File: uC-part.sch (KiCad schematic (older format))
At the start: 21 parts, among them P1 swdio, Q1 Q_PNP_BCE, Q2 Q_PNP_BCE, U4 stm32f042k6tx

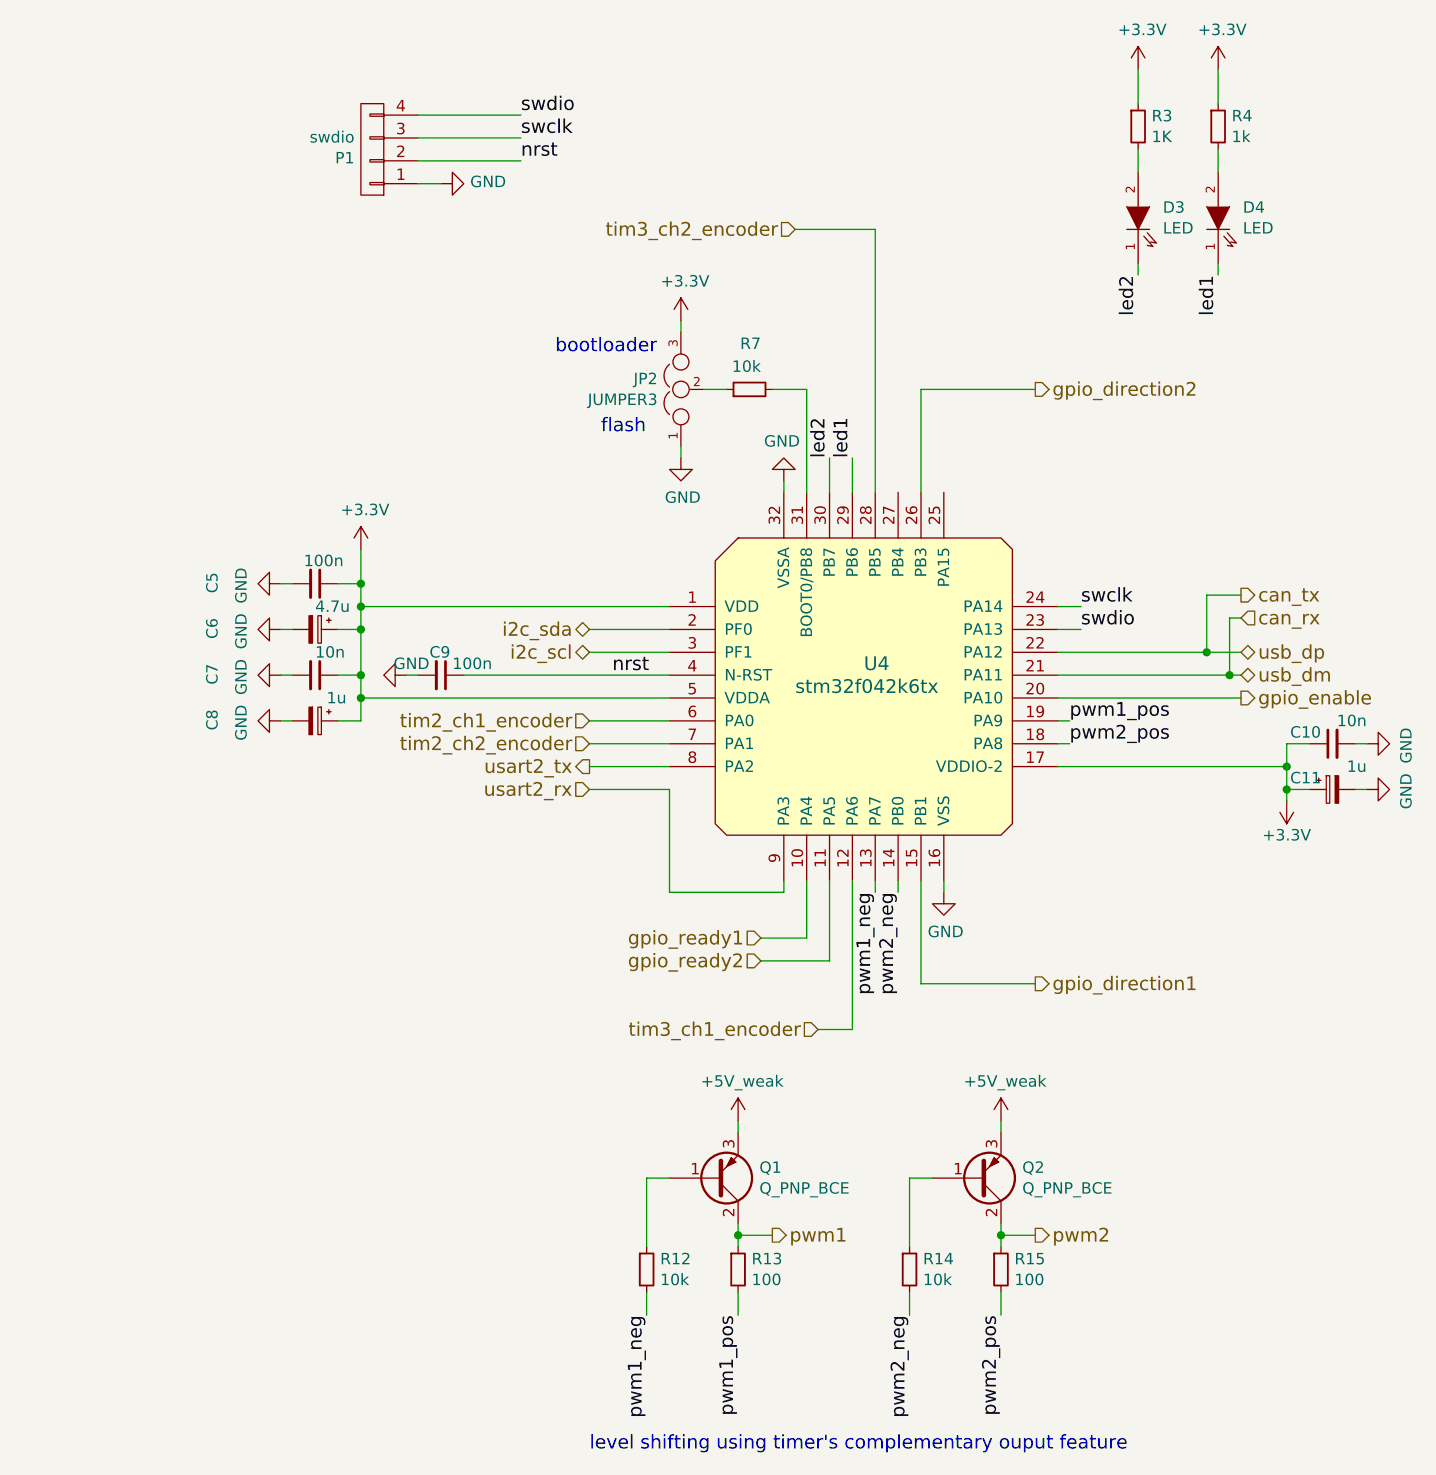
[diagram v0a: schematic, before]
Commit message: schematic seems ok, ongoing routing
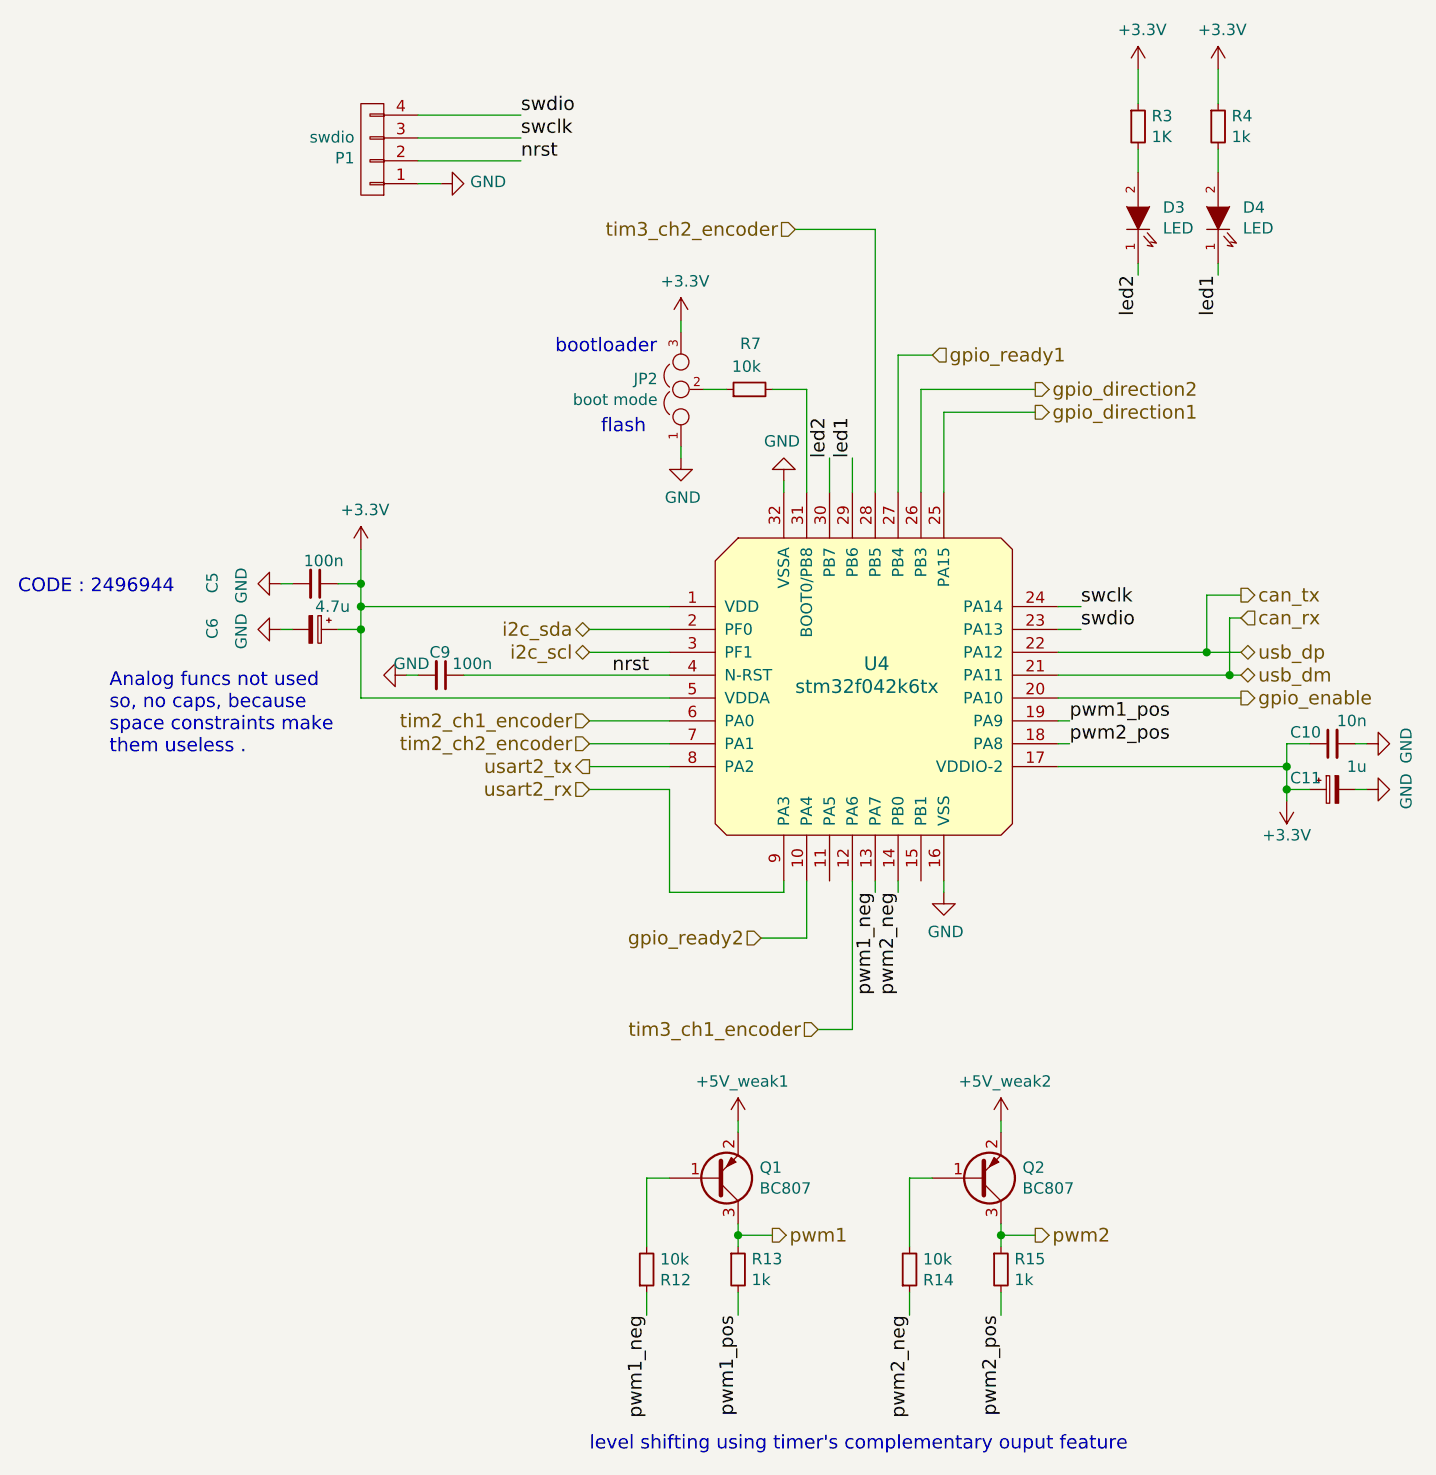
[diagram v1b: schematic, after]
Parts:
- removed C7: 10n, Capacitors_SMD:C_0805, symbol C_Small
- removed C8: 1u, Capacitors_SMD:c_elec_3x5.3, symbol CP_Small
- removed Q1, Q2: Q_PNP_BCE, TO_SOT_Packages_SMD:SOT-23, symbol Q_PNP_BCE
- added Q1, Q2: BC807, TO_SOT_Packages_SMD:SOT-23, symbol Q_PNP_BEC
- C11, C6: footprint Capacitors_SMD:c_elec_3x5.3 -> Capacitors_SMD:C_0805
- D3, D4: footprint LEDs:LED_0603 -> LEDs:LED_0805
- JP2: value JUMPER3 -> boot mode; footprint Pin_Headers:Pin_Header_Straight_1x03_Pitch2.00mm -> de24-2:jumper_switch_3
- R13, R15: value 100 -> 1k
- U4: footprint Housings_QFP:TQFP-32_7x7mm_Pitch0.8mm -> Housings_QFP:LQFP-32_7x7mm_Pitch0.8mm
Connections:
- net gpio_direction1: now also U4.25 (PA15); no longer U4.15 (PB1)
- net gpio_ready1: now also U4.27 (PB4); no longer U4.10 (PA4)
- net gpio_ready2: now also U4.10 (PA4); no longer U4.11 (PA5)
- net pwm1: now also Q1.3 (C)
- net pwm1_neg: now also R12.1; no longer R12.2
- net pwm2: now also Q2.3 (C)
- net pwm2_neg: now also R14.1; no longer R14.2
- new net: Q1.1 (B), R12.2
- new net: Q2.1 (B), R14.2
- new net +5V_weak1: Q1.2 (E)
- new net +5V_weak2: Q2.2 (E)
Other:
- note added: "Analog funcs not used\nso, no caps, because \nspace constraints make\nthem useless ."
- note added: "CODE : 2496944"
